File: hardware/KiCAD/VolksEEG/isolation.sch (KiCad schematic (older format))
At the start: 3 parts

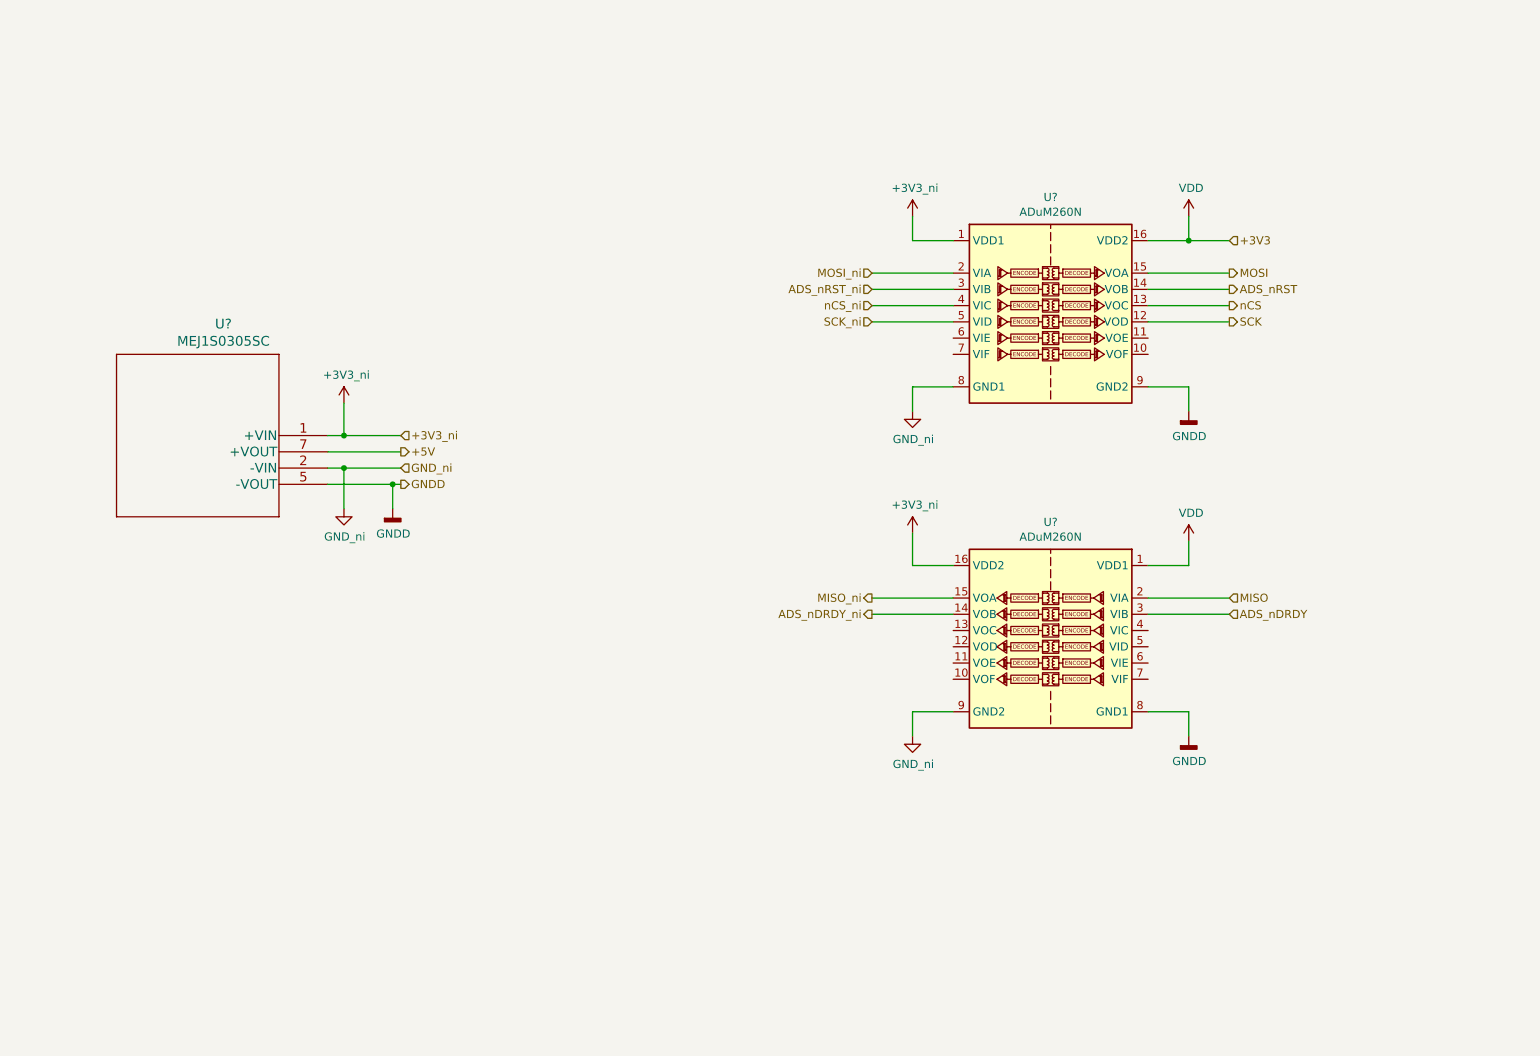
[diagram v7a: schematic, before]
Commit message: Tweaks based on feedback, Changed digital isolators to ADUM240E devices due to component availability.
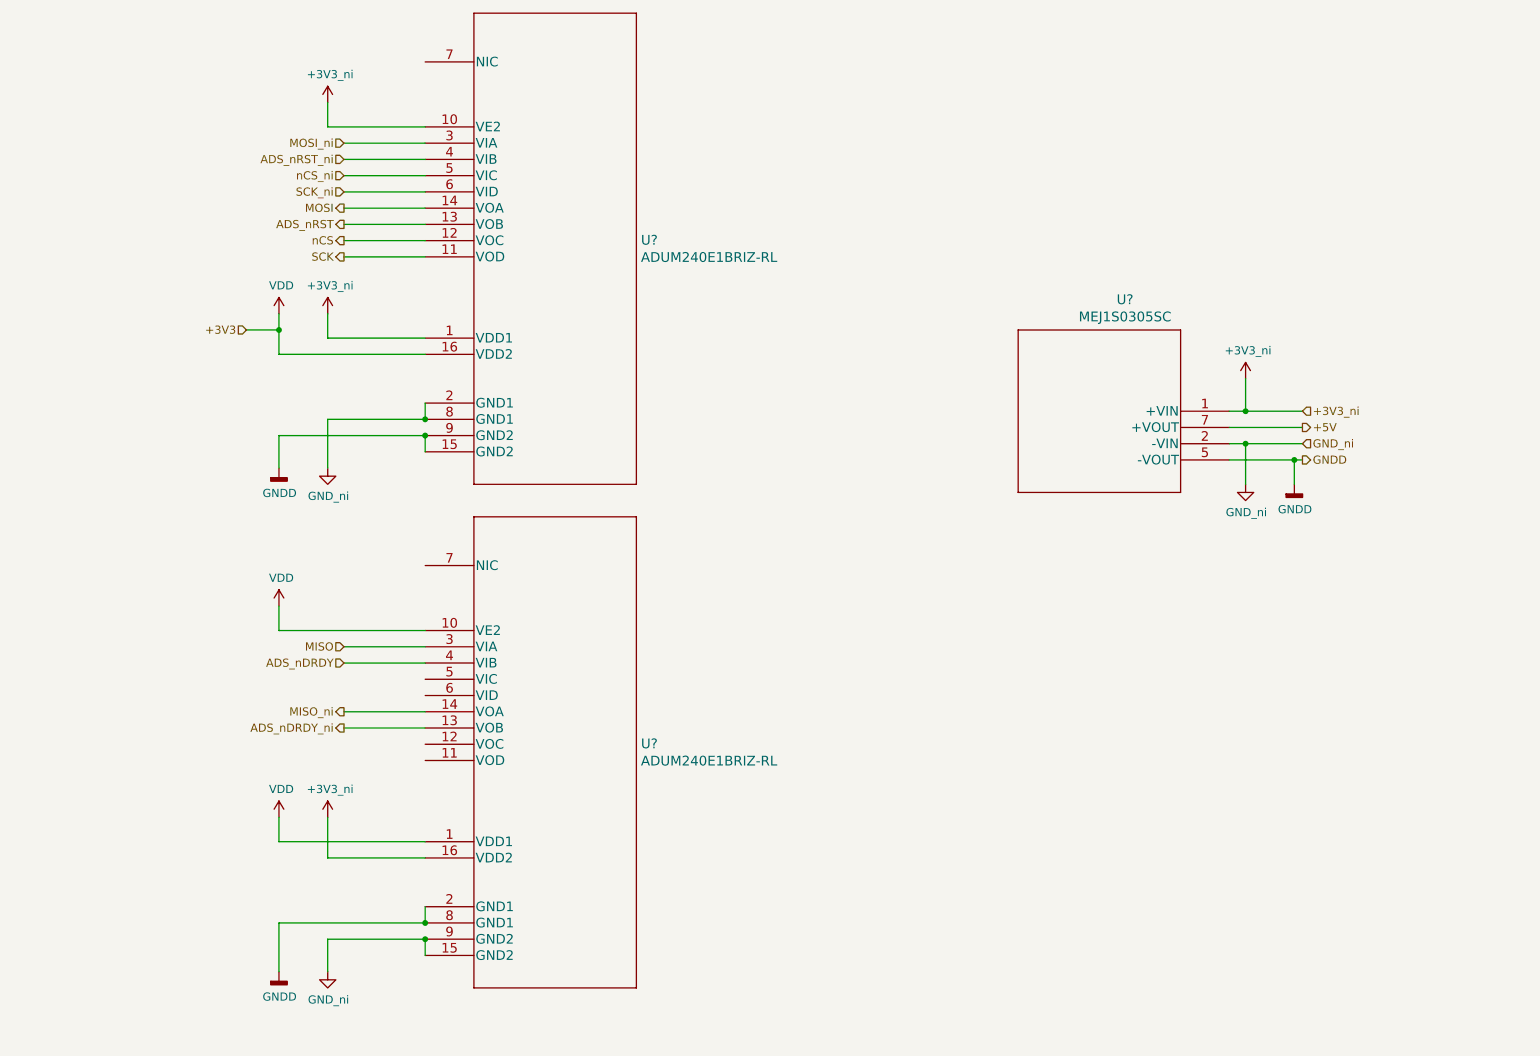
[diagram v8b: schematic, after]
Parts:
- removed U? (x2): ADuM260N, Package_SO:SOIC-16W_7.5x12.8mm_P1.27mm, symbol Isolator:ADuM260N
- added U? (x2): ADUM240E1BRIZ-RL, RI_16_2_ADI, symbol VolksEEG:ADUM240E1BRIZ-RL
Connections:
- net +3V3: now also U?.1 (VDD1), U?.1 (VDD1), U?.10 (VE2), U?.10 (VE2), U?.16 (VDD2), U?.16 (VDD2)
- net ADS_nDRDY: now also U?.4 (VIB)
- net ADS_nDRDY_ni: now also U?.13 (VOB)
- net ADS_nRST: now also U?.13 (VOB)
- net ADS_nRST_ni: now also U?.4 (VIB)
- net GND: now also U?.15 (GND2), U?.2 (GND1), U?.8 (GND1), U?.9 (GND2)
- net GNDD: now also U?.15 (GND2), U?.2 (GND1), U?.8 (GND1), U?.9 (GND2)
- net MISO: now also U?.3 (VIA)
- net MISO_ni: now also U?.14 (VOA)
- net MOSI: now also U?.14 (VOA)
- net MOSI_ni: now also U?.3 (VIA)
- net SCK: now also U?.11 (VOD)
- net SCK_ni: now also U?.6 (VID)
- net nCS: now also U?.12 (VOC)
- net nCS_ni: now also U?.5 (VIC)
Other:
- moved on the sheet: U?
